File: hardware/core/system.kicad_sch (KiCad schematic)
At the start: 2 parts, among them J1 MOLEX_SlimStack_505550-1020, U1 XIAO-NRF54L15

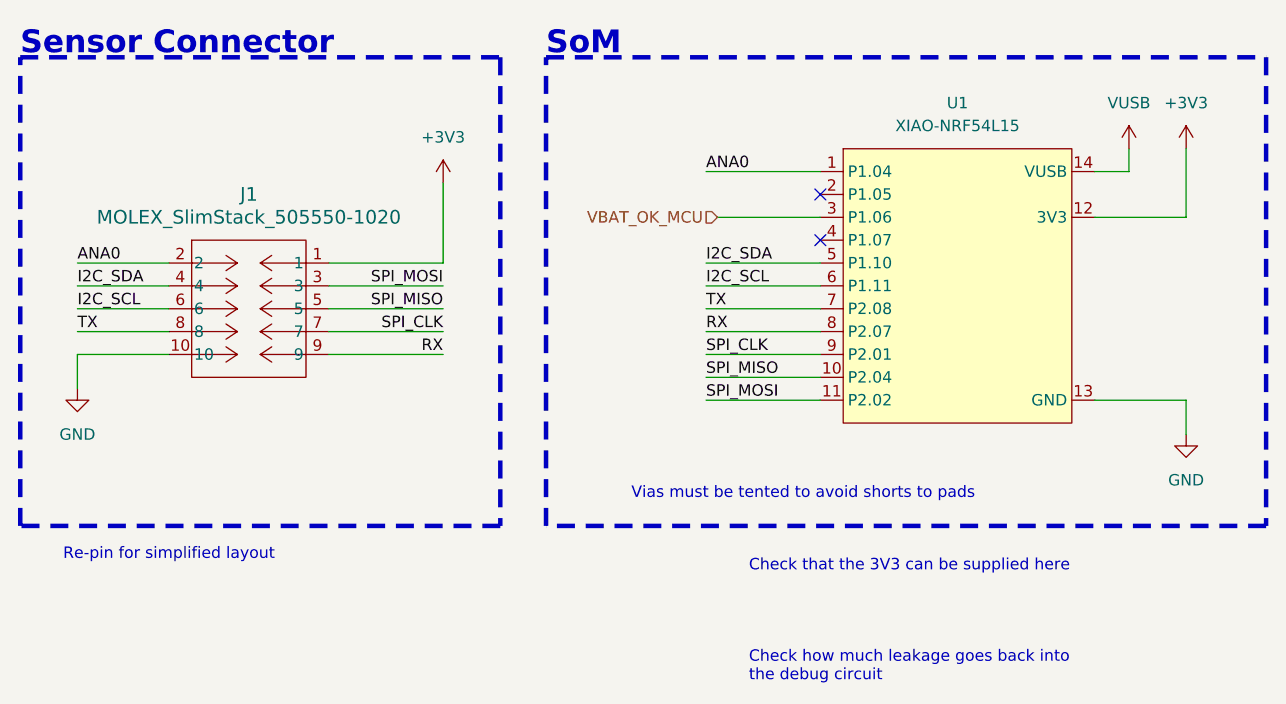
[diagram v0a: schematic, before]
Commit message: updated schematics after some checks to the harvester logic
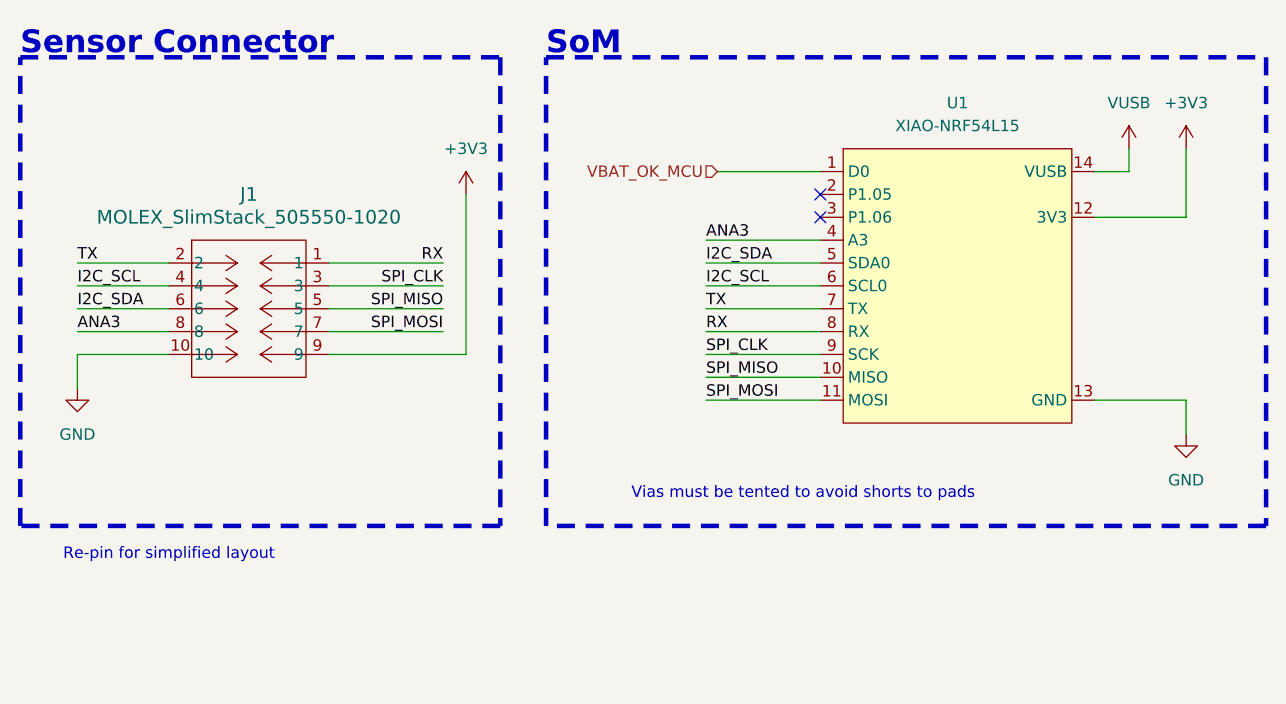
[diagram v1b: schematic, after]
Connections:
- net +3V3: now also J1.9; no longer J1.1
- net I2C_SCL: now also J1.4; no longer J1.6
- net I2C_SDA: now also J1.6; no longer J1.4
- net RX: now also J1.1; no longer J1.9
- net SPI_CLK: now also J1.3; no longer J1.7
- net SPI_MOSI: now also J1.7; no longer J1.3
- net TX: now also J1.2; no longer J1.8
- net VBAT_OK_MCU: now also U1.1 (P1.04); no longer U1.3 (P1.06)
- net ANA3: now reaches U1.4 (P1.07)
- net ANA3: now also J1.8
- removed net ANA0: J1.2, U1.1 (P1.04)

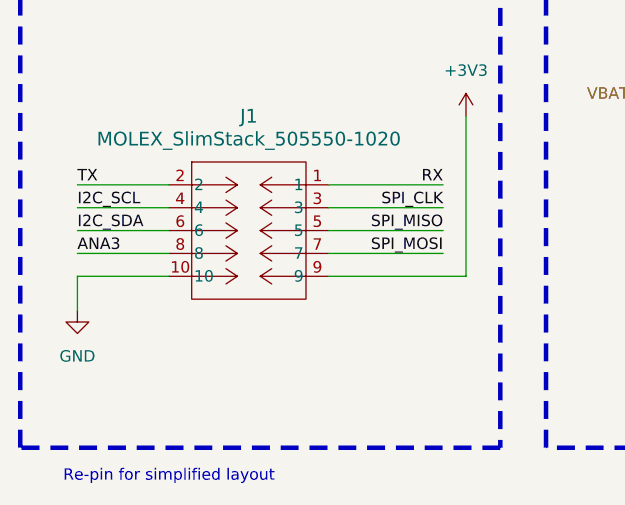
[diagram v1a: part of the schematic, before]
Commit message: Updated with cap and connector
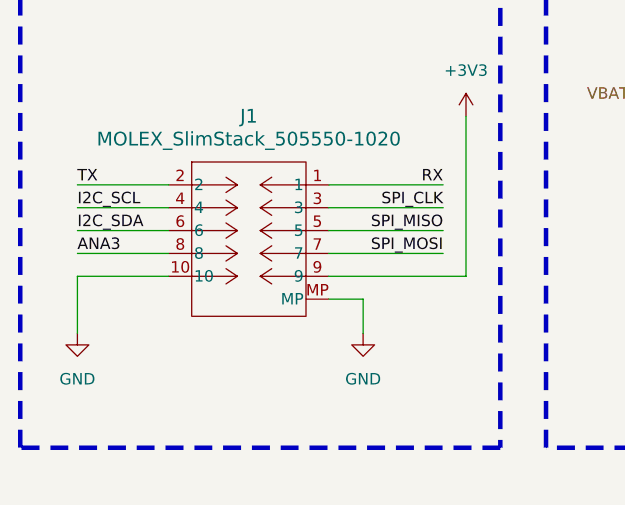
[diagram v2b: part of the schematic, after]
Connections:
- net GND: now also J1.MP
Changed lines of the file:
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@@
-		)
-	)
-	(text_box "Re-pin for simplified layout"
-		(exclude_from_sim no)
-		(at 91.44 127 0)
-		(size 43.18 7.62)
-		(margins 0.9525 0.9525 0.9525 0.9525)
-		(stroke
-			(width -0.0001)
-			(type solid)
-		)
-		(fill
-			(type color)
-			(color 255 0 0 1)
-		)
-		(effects
-			(font
-				(size 1.27 1.27)
-				(color 255 255 255 1)
-			)
-			(justify left top)
 		)
 	)
@@
 	(wire
 		(pts
-			(xy 93.98 110.49) (xy 93.98 106.68)
+			(xy 93.98 113.03) (xy 93.98 106.68)
 		)
 		(stroke
@@
 	(wire
 		(pts
+			(xy 125.73 113.03) (xy 125.73 109.22)
+		)
+		(stroke
+			(width 0)
+			(type default)
+		)
+	)
+	(wire
+		(pts
 			(xy 217.17 111.76) (xy 217.17 115.57)
 		)
@@
 		(pts
 			(xy 137.16 106.68) (xy 121.92 106.68)
+		)
+		(stroke
+			(width 0)
+			(type default)
+		)
+	)
+	(wire
+		(pts
+			(xy 125.73 109.22) (xy 121.92 109.22)
 		)
 		(stroke
@@
 	(symbol
 		(lib_id "power_symbol:GND")
-		(at 93.98 110.49 0)
+		(at 93.98 113.03 0)
 		(unit 1)
 		(exclude_from_sim no)
@@
 		(fields_autoplaced yes)
 		(property "Reference" "#PWR01"
-			(at 93.98 116.84 0)
+			(at 93.98 119.38 0)
 			(effects
 				(font
@@
 		)
 		(property "Value" "GND"
-			(at 93.98 115.57 0)
+			(at 93.98 118.11 0)
 			(effects
 				(font
@@
 		)
 		(property "Footprint" ""
-			(at 93.98 110.49 0)
+			(at 93.98 113.03 0)
 			(effects
 				(font
@@
 		)
 		(property "Datasheet" ""
-			(at 93.98 110.49 0)
+			(at 93.98 113.03 0)
 			(effects
 				(font
@@
 		)
 		(property "Description" "Power symbol creates a global label with name \"GND\" , ground"
-			(at 93.98 110.49 0)
+			(at 93.98 113.03 0)
 			(effects
 				(font
@@
 	)
 	(symbol
+		(lib_id "power_symbol:GND")
+		(at 125.73 113.03 0)
+		(unit 1)
+		(exclude_from_sim no)
+		(in_bom yes)
+		(on_board yes)
+		(dnp no)
+		(fields_autoplaced yes)
+		(property "Reference" "#PWR023"
+			(at 125.73 119.38 0)
+			(effects
+				(font
+					(size 1.27 1.27)
+				)
+				(hide yes)
+			)
+		)
+		(property "Value" "GND"
+			(at 125.73 118.11 0)
+			(effects
+				(font
+					(size 1.27 1.27)
+				)
+			)
+		)
+		(property "Footprint" ""
+			(at 125.73 113.03 0)
+			(effects
+				(font
+					(size 1.27 1.27)
+				)
+				(hide yes)
+			)
+		)
+		(property "Datasheet" ""
+			(at 125.73 113.03 0)
+			(effects
+				(font
+					(size 1.27 1.27)
+				)
+				(hide yes)
+			)
+		)
+		(property "Description" "Power symbol creates a global label with name \"GND\" , ground"
+			(at 125.73 113.03 0)
+			(effects
+				(font
+					(size 1.27 1.27)
+				)
+				(hide yes)
+			)
+		)
+		(pin "1"
+		)
+		(instances
+			(project "core"
+				(path "/8ec7ca4f-74cd-48e1-b45d-8806dcda5073/97f9fe75-9be2-4373-a3aa-3fd324a1345e"
+					(reference "#PWR023")
+					(unit 1)
+				)
+			)
+		)
+	)
+	(symbol
 		(lib_id "power_symbol:+3V3")
 		(at 137.16 88.9 0)
@@
 		(pin "5"
 		)
+		(pin "MP"
+		)
 		(instances

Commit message: updated layout with footprint changes
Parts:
- J1: Part Number (none) -> 5055501020
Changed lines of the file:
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@@
+			)
+		)
+		(property "Part Number" "5055501020"
+			(at 106.68 93.98 0)
+			(effects
+				(font
+					(size 1.27 1.27)
+				)
+				(hide yes)
 			)
 		)

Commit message: added variables
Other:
- note added: "SENSOR CONNECTOR"
- note removed: "Sensor Connector"
- title: (none) -> Xihe
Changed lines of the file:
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@@
 	(generator_version "9.0")
 	(paper "A4")
+	(title_block
+		(title "Xihe")
+		(date "2025-08-19")
+		(rev "0.1")
+	)
 	(rectangle
 		(start 87.63 73.66)
@@
 		)
 	)
-	(text "Sensor Connector"
+	(text "SENSOR CONNECTOR"
 		(exclude_from_sim no)
 		(at 87.63 73.66 0)

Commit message: Minor part choice changes and appropriate board updates
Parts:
- U1: Part Number (none) -> XIAO-NRF54L15

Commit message: bom updates
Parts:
- J1: Manufacturer (none) -> Molex; Mounting Type (none) -> smt
- U1: Manufacturer (none) -> Seeed Studio; Mounting Type (none) -> smt
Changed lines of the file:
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@@
+			)
+		)
+		(property "Manufacturer" "Molex"
+			(at 106.68 93.98 0)
+			(effects
+				(font
+					(size 1.27 1.27)
+				)
+				(hide yes)
+			)
+		)
+		(property "Mounting Type" "smt"
+			(at 106.68 93.98 0)
+			(effects
+				(font
+					(size 1.27 1.27)
+				)
+				(hide yes)
 			)
 		)
@@
 			)
 		)
-		(property "Datasheet" ""
+		(property "Datasheet" "https://wiki.seeedstudio.com/xiao_nrf54l15_sense_getting_started/"
 			(at 179.07 83.82 0)
 			(effects
@@
 			(at 179.07 83.82 0)
 			(effects
+				(font
+					(size 1.27 1.27)
+				)
+				(hide yes)
+			)
+		)
+		(property "Manufacturer" "Seeed Studio"
+			(at 179.07 83.82 0)
+			(effects
+				(font
+					(size 1.27 1.27)
+				)
+				(hide yes)
+			)
+		)
+		(property "Mounting Type" "smt"
+			(at 179.07 83.82 0)
+			(effects
